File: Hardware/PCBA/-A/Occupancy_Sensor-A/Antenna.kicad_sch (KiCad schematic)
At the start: 3 parts

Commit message: Add TOF footprint, component to schematic
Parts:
- C26: footprint (none) -> Capacitor_SMD:C_0402_1005Metric
- L4: footprint (none) -> Inductor_SMD:L_0402_1005Metric
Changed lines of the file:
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@@
       (effects (font (size 1.27 1.27)) (justify left))
     )
-    (property "Footprint" "" (at 67.31 86.36 0)
+    (property "Footprint" "Capacitor_SMD:C_0402_1005Metric" (at 67.31 86.36 0)
       (effects (font (size 1.27 1.27)) hide)
     )
@@
       (effects (font (size 1.27 1.27)))
     )
-    (property "Footprint" "" (at 76.2 78.74 0)
+    (property "Footprint" "Inductor_SMD:L_0402_1005Metric" (at 76.2 78.74 0)
       (effects (font (size 1.27 1.27)) hide)
     )

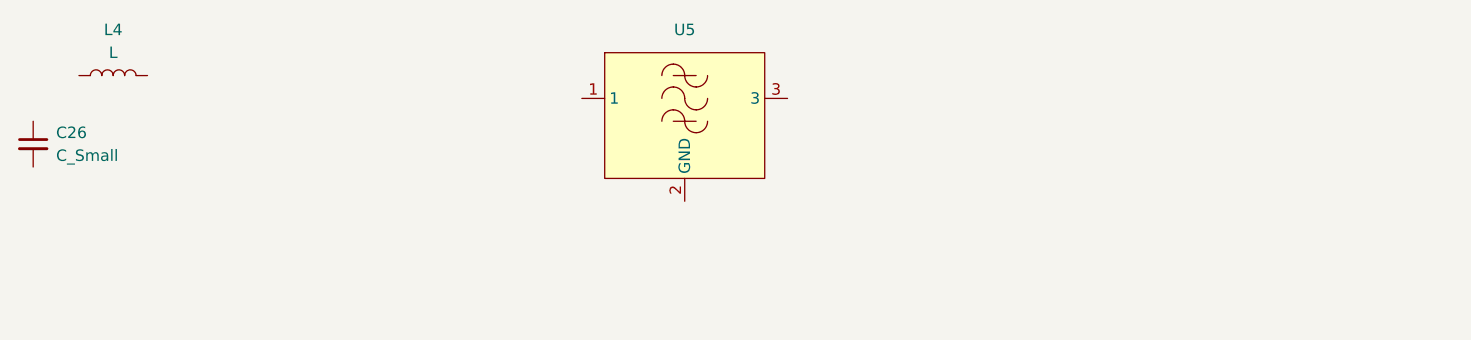
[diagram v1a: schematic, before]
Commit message: Update antenna circuit
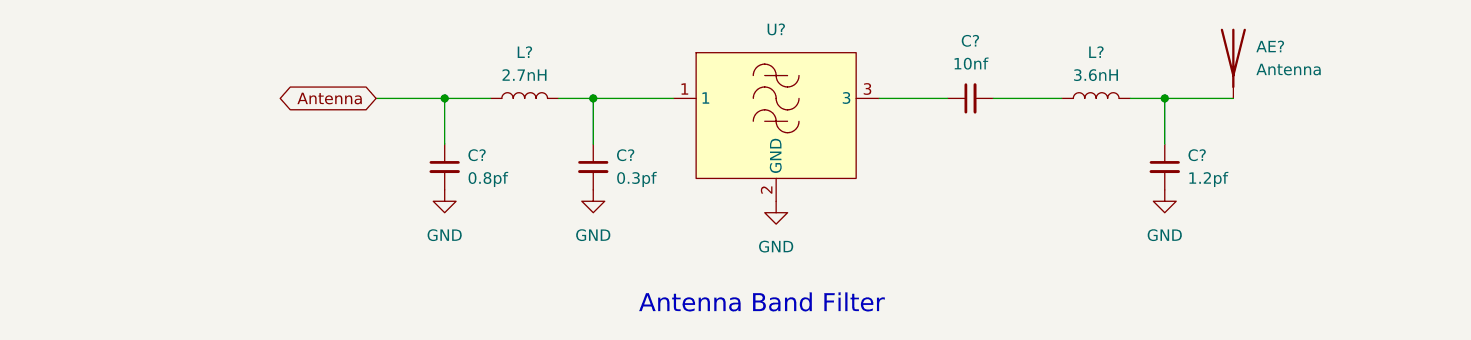
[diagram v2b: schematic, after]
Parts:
- removed C26: C_Small, Capacitor_SMD:C_0402_1005Metric, symbol Device:C_Small
- removed L4: L, Inductor_SMD:L_0402_1005Metric, symbol Device:L
- removed U5: ~, symbol Occupancy_Sensor_Custom_Symbols:LFB182G45CGFD436
- added AE?: Antenna, symbol Device:Antenna
- added C?: 0.8pf, Capacitor_SMD:C_0402_1005Metric, symbol Device:C_Small
- added C?: 0.3pf, Capacitor_SMD:C_0402_1005Metric, symbol Device:C_Small
- added C?: 10nf, Capacitor_SMD:C_0402_1005Metric, symbol Device:C_Small
- added C?: 1.2pf, Capacitor_SMD:C_0402_1005Metric, symbol Device:C_Small
- added L?: 3.6nH, symbol Device:L
- added L?: 2.7nH, symbol Device:L
- added U?: ~, symbol Occupancy_Sensor_Custom_Symbols:LFB182G45CGFD436
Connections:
- new net: AE?.1 (A), C?.1, L?.2
- new net: C?.1, L?.2, U?.1
- new net: C?.2, L?.1
- new net: C?.1, U?.3
- new net Antenna: C?.1, L?.1
- new net GND: C?.2, C?.2, C?.2, U?.2 (GND)
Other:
- note added: "Antenna Band Filter"

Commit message: Adding coaxial connector
Adding coaxial connector.
Remove On board PCB antenna.
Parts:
- removed AE?: Antenna, symbol Device:Antenna
- added J3: Conn_Coaxial, symbol Connector:Conn_Coaxial
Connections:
- net GND: now also J3.2 (Ext)
- net at C?.1, L?.2: now also J3.1 (In)
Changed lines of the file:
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@@
+    (stroke (width 0) (type default))
+  )
+  (wire (pts (xy 205.74 86.36) (xy 205.74 91.44))
     (stroke (width 0) (type default))
   )
@@
     )
   )
-  (symbol (lib_id "Device:Antenna") (at 200.66 76.2 0) (unit 1)
-    (in_bom yes) (on_board yes) (dnp no) (fields_autoplaced)
-    (property "Reference" "AE?" (at 203.2 75.565 0)
-      (effects (font (size 1.27 1.27)) (justify left))
-    )
-    (property "Value" "Antenna" (at 203.2 78.105 0)
-      (effects (font (size 1.27 1.27)) (justify left))
-    )
-    (property "Footprint" "" (at 200.66 76.2 0)
-      (effects (font (size 1.27 1.27)) hide)
-    )
-    (property "Datasheet" "~" (at 200.66 76.2 0)
-      (effects (font (size 1.27 1.27)) hide)
-    )
-    (pin "1")
-    (instances
-      (project "Occupancy_Sensor-A"
-        (path "/65754ac2-2d88-4eb3-8ab1-1eadbd0f428e"
-          (reference "AE?") (unit 1)
-        )
-        (path "/65754ac2-2d88-4eb3-8ab1-1eadbd0f428e/2fdeacbb-ae85-4540-a276-241b92a77837"
-          (reference "AE1") (unit 1)
-        )
-      )
-    )
-  )
   (symbol (lib_id "Device:C_Small") (at 129.54 88.9 0) (unit 1)
     (in_bom yes) (on_board yes) (dnp no) (fields_autoplaced)
@@
         (path "/65754ac2-2d88-4eb3-8ab1-1eadbd0f428e/2fdeacbb-ae85-4540-a276-241b92a77837"
           (reference "C25") (unit 1)
+        )
+      )
+    )
+  )
+  (symbol (lib_id "Connector:Conn_Coaxial") (at 205.74 81.28 0) (unit 1)
+    (in_bom yes) (on_board yes) (dnp no) (fields_autoplaced)
+    (property "Reference" "J3" (at 209.55 80.3032 0)
+      (effects (font (size 1.27 1.27)) (justify left))
+    )
+    (property "Value" "Conn_Coaxial" (at 209.55 82.8432 0)
+      (effects (font (size 1.27 1.27)) (justify left))
+    )
+    (property "Footprint" "" (at 205.74 81.28 0)
+      (effects (font (size 1.27 1.27)) hide)
+    )
+    (property "Datasheet" " ~" (at 205.74 81.28 0)
+      (effects (font (size 1.27 1.27)) hide)
+    )
+    (pin "1")
+    (pin "2")
+    (instances
+      (project "Occupancy_Sensor-A"
+        (path "/65754ac2-2d88-4eb3-8ab1-1eadbd0f428e/2fdeacbb-ae85-4540-a276-241b92a77837"
+          (reference "J3") (unit 1)
         )
       )
@@
         )
       )
+    )
+  )
+  (symbol (lib_id "power:GND") (at 205.74 91.44 0) (unit 1)
+    (in_bom yes) (on_board yes) (dnp no) (fields_autoplaced)
+    (property "Reference" "#PWR?" (at 205.74 97.79 0)
+      (effects (font (size 1.27 1.27)) hide)
+    )
+    (property "Value" "GND" (at 205.74 96.52 0)
+      (effects (font (size 1.27 1.27)))
+    )
+    (property "Footprint" "" (at 205.74 91.44 0)
+      (effects (font (size 1.27 1.27)) hide)
+    )
+    (property "Datasheet" "" (at 205.74 91.44 0)
+      (effects (font (size 1.27 1.27)) hide)
+    )
+    (pin "1")
+    (instances
+      (project "Occupancy_Sensor-A"
+        (path "/65754ac2-2d88-4eb3-8ab1-1eadbd0f428e"
+          (reference "#PWR?") (unit 1)
+        )
+        (path "/65754ac2-2d88-4eb3-8ab1-1eadbd0f428e/2fdeacbb-ae85-4540-a276-241b92a77837"
+          (reference "#PWR068") (unit 1)
+        )
+      )
